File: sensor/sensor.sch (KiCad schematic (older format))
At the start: 3 parts, among them J1 Conn_02x04_Counter_Clockwise, J2 Conn_01x03, U1 KMZ60

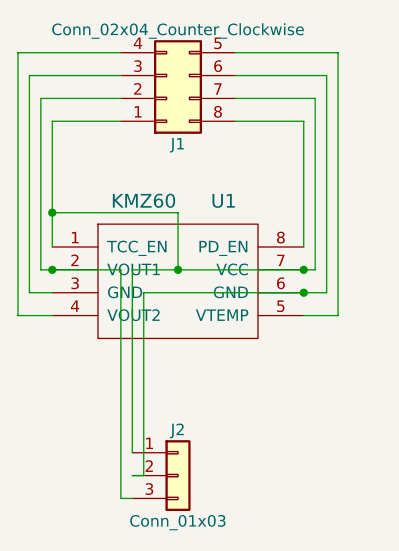
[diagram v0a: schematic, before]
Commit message: sensor board double output update
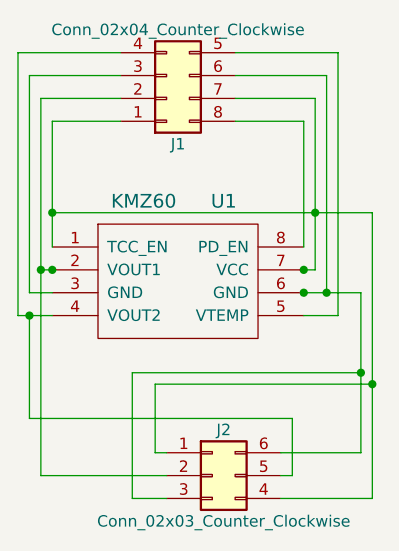
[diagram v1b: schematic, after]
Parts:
- removed J2: Conn_01x03, Pin_Headers:Pin_Header_Straight_1x03_Pitch2.54mm, symbol Conn_01x03
- added J2: Conn_02x03_Counter_Clockwise, Pin_Headers:Pin_Header_Straight_2x03_Pitch2.54mm, symbol Conn_02x03_Counter_Clockwise
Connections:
- net at J1.1 (Pin_1), J1.7 (Pin_7), U1.1 (TCC_EN)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: now also J2.1 (Pin_1), J2.4 (Pin_4)
- net at J1.2 (Pin_2), U1.2 (VOUT1): now also J2.2 (Pin_2)
- net at J1.4 (Pin_4), U1.4 (VOUT2): now also J2.5 (Pin_5)
- net at J1.6 (Pin_6), U1.6 (GND): now also J2.3 (Pin_3), J2.6 (Pin_6)
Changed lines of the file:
@@
 	1    0    0    1
-$EndComp
-$Comp
-L Conn_01x03 J2
-U 1 1 5ACEDC13
-P 5700 4250
-F 0 "J2" H 5700 4450 50  0000 C CNN
-F 1 "Conn_01x03" H 5700 4050 50  0000 C CNN
-F 2 "Pin_Headers:Pin_Header_Straight_1x03_Pitch2.54mm" H 5700 4250 50  0001 C CNN
-F 3 "" H 5700 4250 50  0001 C CNN
-	1    5700 4250
-	1    0    0    -1
 $EndComp
 Wire Wire Line
@@
 	5150 2700 5450 2700
 Wire Wire Line
-	5100 3350 5450 3350
-Wire Wire Line
-	5100 3350 5100 2600
+	5100 2600 5100 4250
 Wire Wire Line
 	5100 2600 5450 2600
@@
 	6250 2700 5950 2700
 Wire Wire Line
-	5500 3350 6300 3350
-Wire Wire Line
 	6300 3350 6300 2600
 Wire Wire Line
 	6300 2600 5950 2600
-Wire Wire Line
-	5550 3450 6350 3450
 Wire Wire Line
 	6350 3450 6350 2500
@@
 Wire Wire Line
 	6400 2400 5950 2400
+Connection ~ 6250 3350
+Connection ~ 6250 3450
+Connection ~ 5150 3350
+Connection ~ 5150 3100
+$Comp
+L Conn_02x03_Counter_Clockwise J2
+U 1 1 5AD54106
+P 5850 4250
+F 0 "J2" H 5900 4450 50  0000 C CNN
+F 1 "Conn_02x03_Counter_Clockwise" H 5900 4050 50  0000 C CNN
+F 2 "Pin_Headers:Pin_Header_Straight_2x03_Pitch2.54mm" H 5850 4250 50  0001 C CNN
+F 3 "" H 5850 4250 50  0001 C CNN
+	1    5850 4250
+	1    0    0    -1
+$EndComp
 Wire Wire Line
-	5500 3350 5500 4150
-Connection ~ 6250 3350
+	6300 3350 6250 3350
+Connection ~ 6300 3100
 Wire Wire Line
-	5550 3450 5550 4250
+	5150 3100 6550 3100
 Wire Wire Line
-	5550 4250 5500 4250
-Connection ~ 6250 3450
+	6500 3450 6500 4150
 Wire Wire Line
-	5450 4350 5500 4350
+	6500 4150 6150 4150
+Connection ~ 6350 3450
 Wire Wire Line
-	5450 3350 5450 4350
-Connection ~ 5150 3350
+	6500 3800 5500 3800
 Wire Wire Line
-	5150 3100 5700 3100
+	5500 3800 5500 4350
 Wire Wire Line
-	5700 3100 5700 3350
-Connection ~ 5700 3350
-Connection ~ 5150 3100
+	5500 4350 5650 4350
+Connection ~ 6500 3800
+Wire Wire Line
+	5100 3350 5150 3350
+Wire Wire Line
+	6250 3450 6500 3450
+Wire Wire Line
+	6550 3100 6550 4350
+Wire Wire Line
+	6550 4350 6150 4350
+Wire Wire Line
+	5650 4150 5600 4150
+Wire Wire Line
+	5600 4150 5600 3850
+Wire Wire Line
+	5600 3850 6550 3850
+Connection ~ 6550 3850
+Wire Wire Line
+	5100 4250 5650 4250
+Connection ~ 5100 3350
+Wire Wire Line
+	5050 3550 5050 4000
+Wire Wire Line
+	5050 4000 6200 4000
+Wire Wire Line
+	6200 4000 6200 4250
+Wire Wire Line
+	6200 4250 6150 4250
+Connection ~ 5050 3550
 $EndSCHEMATC
